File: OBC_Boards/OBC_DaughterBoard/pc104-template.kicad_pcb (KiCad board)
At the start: 4 copper layers, 99.3 x 122.9 mm, 52 parts, among them J1 PC104_Connector, J2 ST11S008V4HR2000, J3 Conn_02x20_Odd_Even, J4 3.3V Input (Testing), J5 5V Input (Testing), J6 Conn_02x06_Odd_Even, J7 Conn_01x04, J8 Conn_01x04, J9 Conn_01x04, Q1 Q_PMOS_DGS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

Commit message: temp sensor footprint
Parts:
- added BT2: BVSD-2032-PC, Daughterboard_footprints:BAT_BVSD-2032-PC, F.Cu at (31.8, 99.3)
- added C10: 18pF, Daughterboard_footprints:CAPC1608X90N, F.Cu at (52.3, 88.3)
- added C11: 10uF, Daughterboard_footprints:CAPC1608X90N, F.Cu at (52.3, 90.8)
- added C4: 0.1uF, Daughterboard_footprints:CAPC1608X90N, F.Cu at (47.9, 124.2)
- added C5: 10uF, Daughterboard_footprints:CAPC1608X90N, F.Cu at (47.9, 126.6)
- added C9: 18pF, Daughterboard_footprints:CAPC1608X90N, F.Cu at (48.3, 90.8)
- added D4: RED, Daughterboard_footprints:CAPC1608X90N, F.Cu at (47.9, 121.7)
- added D6: RED, Daughterboard_footprints:CAPC1608X90N, F.Cu at (56.3, 88.3)
- added FB3: 100R @ 100 MHz, Daughterboard_footprints:BEADC1608X75N, F.Cu at (74.6, 129.6)
- added FB4: 100R @ 100 MHz, Daughterboard_footprints:BEADC1608X75N, F.Cu at (29.7, 141.2)
- added FB5: 100R @ 100 MHz, Daughterboard_footprints:BEADC1608X75N, F.Cu at (70.2, 91.6)
- added FB6: 100R @ 100 MHz, Daughterboard_footprints:BEADC1608X75N, F.Cu at (82.3, 121.7)
- added FB7: 100R @ 100 MHz, Daughterboard_footprints:BEADC1608X75N, F.Cu at (29.7, 114.6)
- added J10: Conn_01x04, Connector_PinHeader_2.54mm:PinHeader_1x04_P2.54mm_Vertical, F.Cu at (65.6, 122.8)
- added J2: ST11S008V4HR2000, STM32_Breakout:ST11S008V4HR2000, F.Cu at (35.4, 131.5)
- added J9: Conn_01x04, Connector_PinHeader_2.54mm:PinHeader_1x04_P2.54mm_Vertical, F.Cu at (70.2, 122.8)
- added R1: 100m, Resistor_SMD:R_0201_0603Metric, F.Cu at (81.5, 123.8)
- added R10: 2.2k, Daughterboard_footprints:RESC1608X55N, F.Cu at (33.7, 141.1)
- added R11: 33, Daughterboard_footprints:RESC1608X55N, F.Cu at (51.9, 121.7)
- added R12: 100m, Resistor_SMD:R_0201_0603Metric, F.Cu at (75.6, 87.9)
- added R14: 2.2k, Daughterboard_footprints:RESC1608X55N, F.Cu at (48.3, 88.3)
- added R2: 10k, Daughterboard_footprints:RESC1608X55N, F.Cu at (74.5, 132.1)
- added R3: 10k, Daughterboard_footprints:RESC1608X55N, F.Cu at (78.6, 129.6)
- added R4: 10k, Daughterboard_footprints:RESC1608X55N, F.Cu at (80.7, 126.2)
- added TP1: TestPoint, TestPoint:TestPoint_2Pads_Pitch2.54mm_Drill0.8mm, F.Cu at (74.4, 126.7)
- added TP2: TestPoint, TestPoint:TestPoint_2Pads_Pitch2.54mm_Drill0.8mm, F.Cu at (70.1, 88.7)
- added U2: MCP9808T-E/MC, Daughterboard_footprints:SOP65P490X110-8N, F.Cu at (76.7, 122.7)
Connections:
- net 5V_CHG renamed BatVBUS
- D3 pad 1: Net-(D3-Pad1) -> Net-(C3-Pad1)
- FB1 pad 2: 5V_VC_Input -> 5V_Rpi_Input
- FB2 pad 1: Net-(D3-Pad1) -> Net-(C3-Pad1)
- J1 pad 1: unconnected-(J1-Pad1) -> COMM_TXD
- J1 pad 100: unconnected-(J1-Pad100) -> GND
- J1 pad 2: unconnected-(J1-Pad2) -> COMM_RXD
- J1 pad 3: unconnected-(J1-Pad3) -> COMM_CTS
- J1 pad 32: unconnected-(J1-Pad32) -> 5VUSB_CHG
- J1 pad 4: unconnected-(J1-Pad4) -> COMM_RTS
- J1 pad 41: unconnected-(J1-Pad41) -> I2C_SDA1
- J1 pad 43: unconnected-(J1-Pad43) -> I2C_SCK1
- J1 pad 5: unconnected-(J1-Pad5) -> ADCS_INT
- J1 pad 6: unconnected-(J1-Pad6) -> EPS_INT
- J1 pad 61: unconnected-(J1-Pad61) -> GND
- J1 pad 66: unconnected-(J1-Pad66) -> GND
- J1 pad 68: unconnected-(J1-Pad68) -> 5V_Debug_Input
- J1 pad 69: unconnected-(J1-Pad69) -> GND
- J1 pad 7: unconnected-(J1-Pad7) -> BAT_INT
- J1 pad 73: unconnected-(J1-Pad73) -> GND
- J1 pad 74: unconnected-(J1-Pad74) -> GND
- J1 pad 77: 5V_BInput -> unconnected-(J1-Pad77)
- J1 pad 8: unconnected-(J1-Pad8) -> OBC_INT
- J1 pad 82: unconnected-(J1-Pad82) -> GND
- J1 pad 84: unconnected-(J1-Pad84) -> GND
- J1 pad 99: unconnected-(J1-Pad99) -> GND
- J3 pad 1: +3V3 -> 3V3
- J3 pad 15: unconnected-(J3-Pad15) -> UART_CTS
- J3 pad 16: unconnected-(J3-Pad16) -> UART_RTS
- J3 pad 29: unconnected-(J3-Pad29) -> GPIO5
- J3 pad 31: unconnected-(J3-Pad31) -> GPIO6
- J3 pad 32: unconnected-(J3-Pad32) -> GPIO12
- J3 pad 33: unconnected-(J3-Pad33) -> GPIO13
- J3 pad 35: unconnected-(J3-Pad35) -> GPIO19
- J6 pad 2: 5V_DInput -> 5V_Debug_Input
- R7 pad 2: GPIO_pin -> Analog_Voltage
- R8 pad 2: GPIO_pin -> Analog_Voltage
- S1 pad P: unconnected-(S1-PadP) -> 5V_Debug_Input
- S1 pad S: unconnected-(S1-PadS) -> 5V_Rpi_Input

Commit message: Fixed libraries path for current monitor in OBC DB
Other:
- board size 99.3 x 122.9 mm -> 90.2 x 95.9 mm

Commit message: obc: daughterboard: clean up all schematics for easier reworks
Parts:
- removed BT1: BVSD-2032-PC, Daughterboard_footprints:BAT_BVSD-2032-PC
- removed the C4 at (47.9, 124.2)
- removed the C4 at (254.5, 136.8)
- removed the C5 at (234.6, 144.8)
- removed the C5 at (47.9, 126.6)
- removed C6, C8: 10uF, Daughterboard_footprints:CAPC1608X90N
- removed C7: 0.1uF, Daughterboard_footprints:CAPC1608X90N
- removed the FB3 at (226.5, 144.9)
- removed the FB3 at (74.6, 129.6)
- removed the FB4 at (29.7, 141.2)
- removed the FB4 at (230.6, 144.9)
- removed G1: CR2032H, CR2032H:CR2032H
- removed J10: Conn_01x04, Connector_PinHeader_2.54mm:PinHeader_1x04_P2.54mm_Vertical
- removed the J2 at (190.4, 82.1)
- removed the J2 at (35.4, 131.5)
- removed the J9 at (245.5, 137.9)
- removed the J9 at (70.2, 122.8)
- removed the R1 at (219.2, 30.9)
- removed the R1 at (81.5, 123.8)
- removed the R10 at (33.7, 141.1)
- removed the R10 at (241.6, 56.3)
- removed the R10 at (238.5, 144.8)
- removed the R2 at (73.7, 48.3)
- removed the R2 at (74.5, 132.1)
- removed the R3 at (81.3, 38.1)
- removed the R3 at (78.6, 129.6)
- removed the R4 at (71.0, 33.2)
- removed the R4 at (80.7, 126.2)
- removed the R7 at (226.5, 147.4)
- removed the R7 at (258.4, 45.0)
- removed the U2 at (76.7, 122.7)
- removed the U2 at (178.8, 29.5)
- removed U3: BU33SA5WGWZ-E2-qsat-symb, STM32_Breakout:BU33SA5WGWZ-E2
- removed U5: MCP3008, MCP3008:Microchip-MCP3008-I_P-Manufacturer_Recommended
- removed U6: JS102011SCQN, Daughterboard_footprints:JS102011SCQN
- removed Y1: CM9V-T1A, CM9V-T1A-32:XTAL_CM9V-T1A-32.768KHZ-9PF-20PPM-TA-QC
- added C4: 0.1uF, Daughterboard_footprints:CAPC1608X90N, F.Cu at (222.5, 91.5)
- added C5: 10uF, Daughterboard_footprints:CAPC1608X90N, F.Cu at (226.5, 89.0)
- added FB3: 100R @ 100 MHz, Daughterboard_footprints:BEADC1608X75N, F.Cu at (133.9, 101.5)
- added FB4: 100R @ 100 MHz, Daughterboard_footprints:BEADC1608X75N, F.Cu at (222.5, 89.0)
- added J2: ST11S008V4HR2000, STM32_Breakout:ST11S008V4HR2000, F.Cu at (224.2, 125.0)
- added J9: Conn_01x04, Connector_PinHeader_2.54mm:PinHeader_1x04_P2.54mm_Vertical, F.Cu at (79.8, 119.9)
- added MAX4372F2: MAX4372FESA+, Daughterboard_footprints:Maxim-MAX4372FESA+-Level_A, F.Cu at (202.3, 103.8)
- added R1: 2.2k, Daughterboard_footprints:RESC1608X55N, F.Cu at (143.2, 108.5)
- added R10: 2.2k, Daughterboard_footprints:RESC1608X55N, F.Cu at (139.2, 158.8)
- added R2: 10k, Daughterboard_footprints:RESC1608X55N, F.Cu at (93.4, 113.7)
- added R3: 10k, Daughterboard_footprints:RESC1608X55N, F.Cu at (84.1, 126.0)
- added R4: 10k, Daughterboard_footprints:RESC1608X55N, F.Cu at (67.6, 159.6)
- added R7: 20k, Daughterboard_footprints:RESC1608X55N, F.Cu at (120.9, 120.3)
- added U2: BU33SA5WGWZ-E2-qsat-symb, STM32_Breakout:BU33SA5WGWZ-E2, F.Cu at (122.8, 104.9)
- added Y2: CM9V-T1A, Daughterboard_footprints:XTAL_CM9V-T1A-32.768KHZ-9PF-20PPM-TA-QC, F.Cu at (181.8, 106.6)
- C1: value 10uF -> 0.1uF
- C2: value 22uF -> 10uF
- C3: value 0.1uF -> 22uF
- D1: value D_Zener -> RED; footprint STM32_Breakout:SOT91P240X110-3N -> Daughterboard_footprints:CAPC1608X90N
- D2: value RED -> D_Zener; footprint Daughterboard_footprints:CAPC1608X90N -> STM32_Breakout:SOT91P240X110-3N
- MAX4372F1: footprint Max4372:Maxim-MAX4372FESA+-Level_A -> Daughterboard_footprints:Maxim-MAX4372FESA+-Level_A
- R9: value 2.2k -> 100m; footprint Daughterboard_footprints:RESC1608X55N -> Resistor_SMD:R_0201_0603Metric
- U1: value MCP79400T-I/SN -> MCP9808T-E/MC; footprint RTC Footprint:SOIC127P600X175-8N -> Daughterboard_footprints:SOP65P490X110-8N
- U4: value JS102011SCQN -> MCP79400T-I/SN; footprint Daughterboard_footprints:JS102011SCQN -> Daughterboard_footprints:SOIC127P600X175-8N
- moved J7 176.0 mm to (75.1, 119.9)
- moved J5 174.6 mm to (89.0, 119.9)
- moved S1 172.8 mm to (72.0, 155.7)
- moved J8 171.8 mm to (91.0, 102.5)
- moved FB7 153.0 mm to (182.1, 101.5)
- moved R5 152.5 mm to (120.9, 117.8)
- moved TP1 147.8 mm to (220.1, 101.9)
- moved C2 147.3 mm to (128.6, 105.9)
- moved R8 144.1 mm to (126.2, 110.9)
- moved D3 143.4 mm to (130.2, 108.4)
- moved R6 140.9 mm to (125.0, 115.3)
- moved FB5 139.1 mm to (209.0, 101.5)
- moved FB6 139.1 mm to (220.3, 104.8)
- moved J4 135.1 mm to (84.4, 119.9)
- moved C10 134.4 mm to (186.1, 101.5)
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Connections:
- D2 pad 1: Net-(C1-Pad1) -> Net-(C2-Pad1)
- D3 pad 1: Net-(C3-Pad1) -> Net-(C2-Pad1)
- FB1 pad 1: Net-(FB1-Pad1) -> Net-(C1-Pad1)
- FB1 pad 2: 5V_Rpi_Input -> +3V3
- FB2 pad 1: Net-(C3-Pad1) -> Net-(FB2-Pad1)
- FB2 pad 2: +3V3 -> 5V_Rpi_Input
- FB6 pad 1: PM_Input -> Net-(FB6-Pad1)
- FB6 pad 2: Net-(FB6-Pad2) -> +3V3
- J4 pad 1: PM_Input -> 3V3
- MAX4372F1 pad 1: Net-(FB3-Pad1) -> Net-(FB6-Pad1)
- MAX4372F1 pad 8: Net-(MAX4372F1-Pad8) -> 3V3
- Q1 pad 1: Net-(FB1-Pad1) -> Net-(FB2-Pad1)
- Q1 pad 2: Net-(D1-Pad2) -> Net-(D2-Pad2)
- Q1 pad 3: Net-(C1-Pad1) -> Net-(C2-Pad1)
- R5 pad 1: Net-(D1-Pad2) -> Net-(D2-Pad2)
- R6 pad 1: Net-(D2-Pad2) -> Net-(D3-Pad2)
- R9 pad 1: Net-(D3-Pad2) -> 3V3
- R9 pad 2: GND -> +3V3
- U1 pad 1: Net-(C5-Pad2) -> /Temperature Sensor/I2C_SDA1
- U1 pad 2: Net-(C4-Pad2) -> /Temperature Sensor/I2C_SCK1
- U1 pad 5: I2C_SDA1 -> GND
- U1 pad 6: I2C_SCL1 -> GND
- U1 pad 7: Net-(R2-Pad2) -> GND
- U1 pad 8: +3.3V -> Net-(C1-Pad1)
- U4 pad 1: unconnected-(U4-Pad1) -> XCO1
- U4 pad 2: 5V_Rpi_Input -> XCO2
- U4 pad 3: 5V_SInput -> VCC_BAT

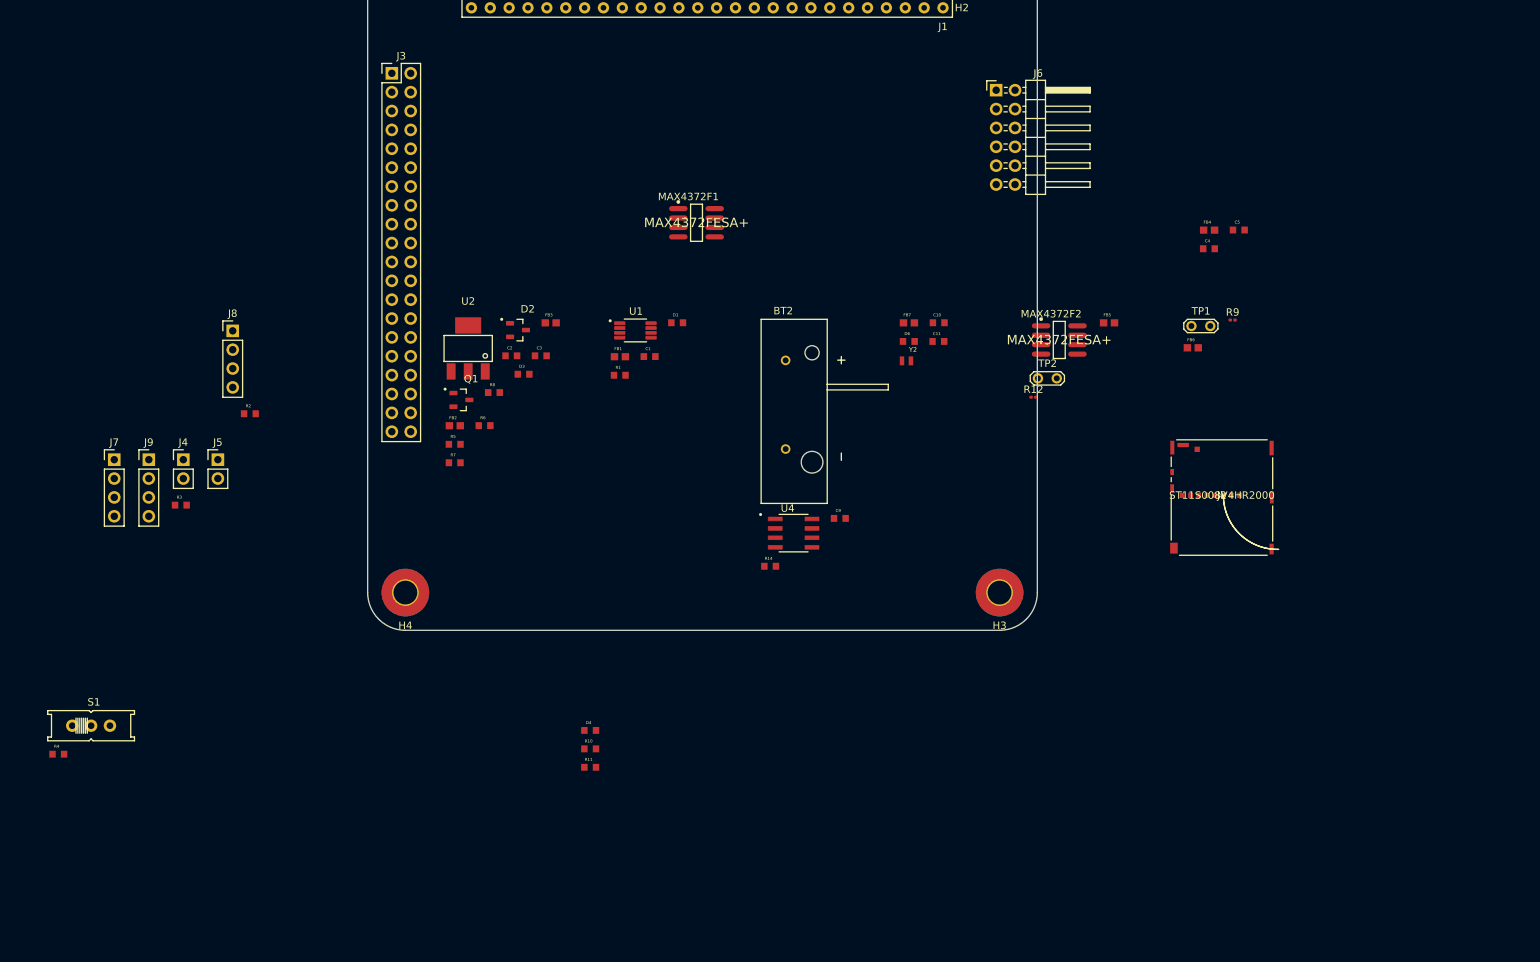
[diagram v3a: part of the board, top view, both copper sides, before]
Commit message: footprint fix
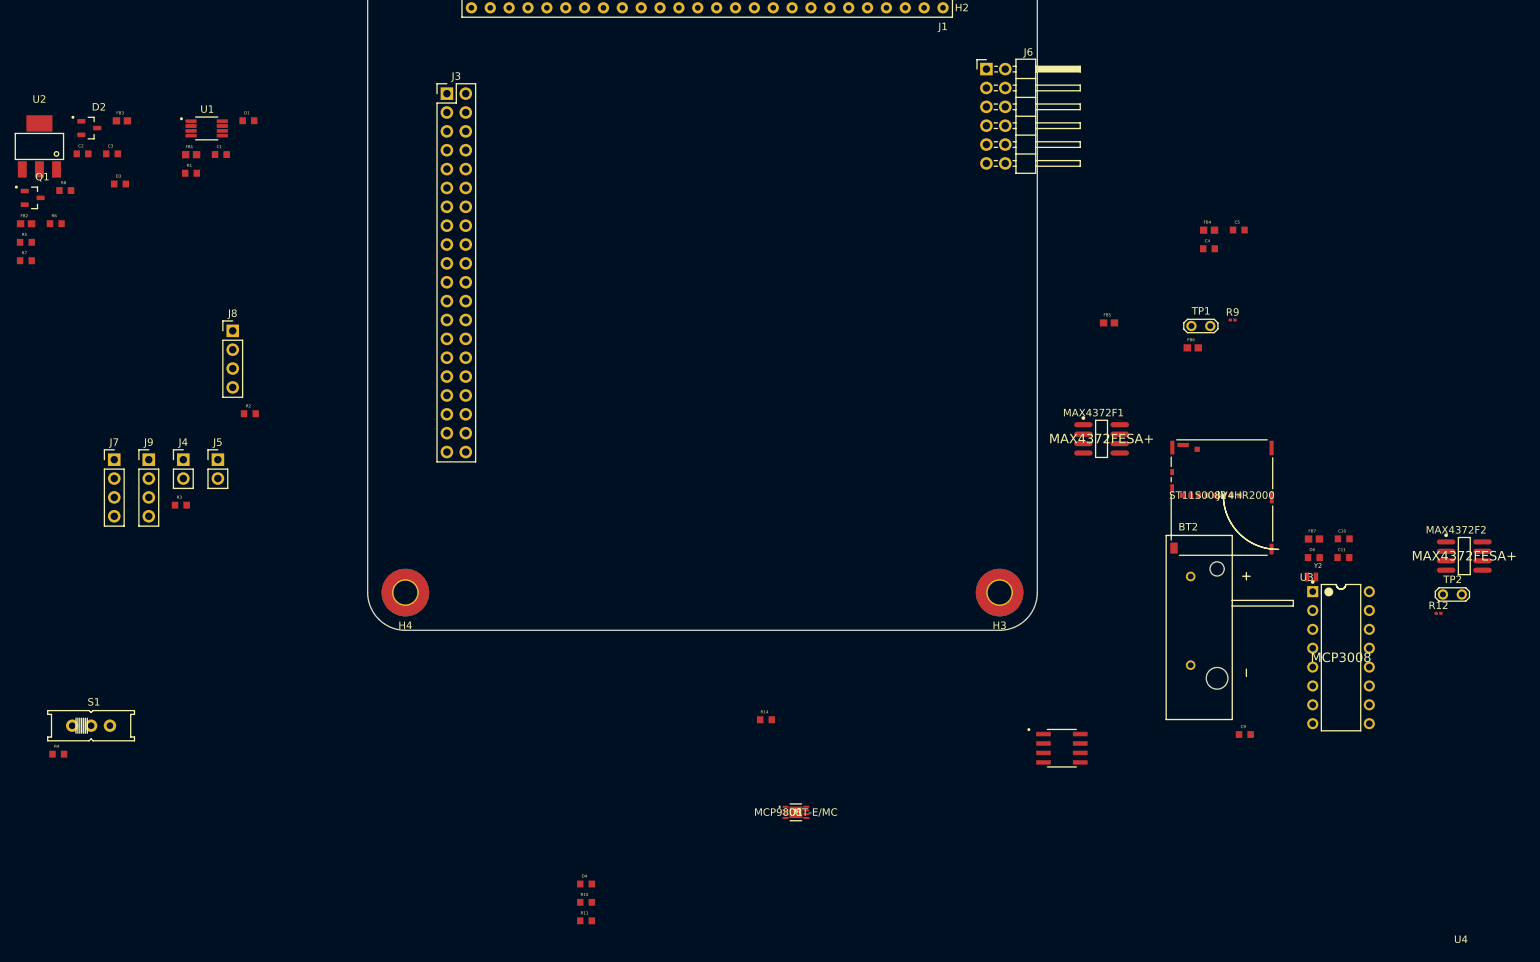
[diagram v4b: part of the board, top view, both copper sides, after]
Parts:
- added U1: MCP9808T-E/MC, Daughterboard_footprints:MCP9808T-E&slash_MC, F.Cu at (166.9, 167.4)
- added U3: MCP3008, Daughterboard_footprints:Microchip-MCP3008-I_P-Manufacturer_Recommended, F.Cu at (240.3, 146.6)
- J3: value Conn_02x20_Odd_Even -> Raspberry Pi 4 Connector
- J6: value Conn_02x06_Odd_Even -> Test Connector
- J7: value Conn_01x04 -> Temp Sens1 Connector
- J8: value Conn_01x04 -> Temp Sens2 Connector
- moved C1 63.8 mm to (89.5, 78.8)
- moved C2 63.8 mm to (70.8, 78.7)
- moved C3 63.8 mm to (74.8, 78.7)
- moved D1 63.8 mm to (93.2, 74.3)
- moved D2 63.8 mm to (71.7, 75.2)
- moved FB1 63.8 mm to (85.5, 78.8)
- moved FB3 63.8 mm to (76.1, 74.3)
- moved U1 63.8 mm to (87.5, 75.3)
- moved FB2 63.8 mm to (63.2, 88.1)
- moved R5 63.8 mm to (63.2, 90.6)
- moved R7 63.8 mm to (63.2, 93.1)
- moved Q1 63.8 mm to (64.1, 84.6)
- moved R1 63.8 mm to (85.4, 81.3)
- moved R6 63.8 mm to (67.2, 88.1)
- moved R8 63.8 mm to (68.5, 83.7)
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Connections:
- net /Real Time Clock/I2C_SCK1 renamed /Real Time Clock/I2C_SCL1
- net Analog_Voltage renamed Net-(R7-Pad2)
- FB2 pad 2: 5V_Rpi_Input -> /PowerConverter/5V0_Input
- FB3 pad 1: 3V3 -> +3V3
- H1 pad 1: unconnected-(H1-Pad1) -> GND
- H2 pad 1: unconnected-(H2-Pad1) -> GND
- H3 pad 1: unconnected-(H3-Pad1) -> GND
- H4 pad 1: unconnected-(H4-Pad1) -> GND
- J1 pad 43: I2C_SCK1 -> I2C_SCL1
- J1 pad 68: 5V_Debug_Input -> SW7_5V_Input
- J3 pad 1: 3V3 -> +3V3
- J3 pad 10: UART_RXD0 -> COMM_RXD
- J3 pad 15: UART_CTS -> COMM_CTS
- J3 pad 16: UART_RTS -> COMM_RTS
- J3 pad 2: 5V_Rpi_Input -> +5V
- J3 pad 4: 5V_Rpi_Input -> +5V
- J3 pad 8: UART_TXD0 -> COMM_TXD
- J4 pad 1: 3V3 -> PM_Input
- J6 pad 2: 5V_Debug_Input -> SW7_5V_Input
- MAX4372F1 pad 8: 3V3 -> PM_Input
- R3 pad 2: I2C_SCK1 -> I2C_SCL1
- R9 pad 1: 3V3 -> PM_Input

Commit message: first commit
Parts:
- removed J9: Conn_01x04, Connector_PinHeader_2.54mm:PinHeader_1x04_P2.54mm_Vertical
- R2, R3, R4: footprint Daughterboard_footprints:RESC1608X55N -> ESR03EZPF1002:RESC1608X55N
- moved S1 152.5 mm to (192.4, 62.2)
- moved R12 132.3 mm to (128.8, 96.1)
- moved C2 112.6 mm to (183.4, 82.5)
- moved R7 111.9 mm to (174.8, 85.7)
- moved J4 111.7 mm to (195.6, 109.2)
- moved FB3 109.9 mm to (184.8, 90.8)
- moved D3 107.7 mm to (183.5, 85.7)
- moved FB2 107.6 mm to (170.8, 87.5)
- moved D2 107.6 mm to (179.3, 74.6)
- moved C3 107.6 mm to (182.4, 78.1)
- moved R8 107.6 mm to (176.1, 83.1)
- moved C10 107.5 mm to (138.6, 96.5)
- moved C11 107.5 mm to (138.6, 99.1)
- moved FB7 107.5 mm to (134.6, 96.6)
- moved Y2 107.5 mm to (134.3, 101.7)
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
